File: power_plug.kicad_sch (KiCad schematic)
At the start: 21 parts, among them K13 Conn_02x03

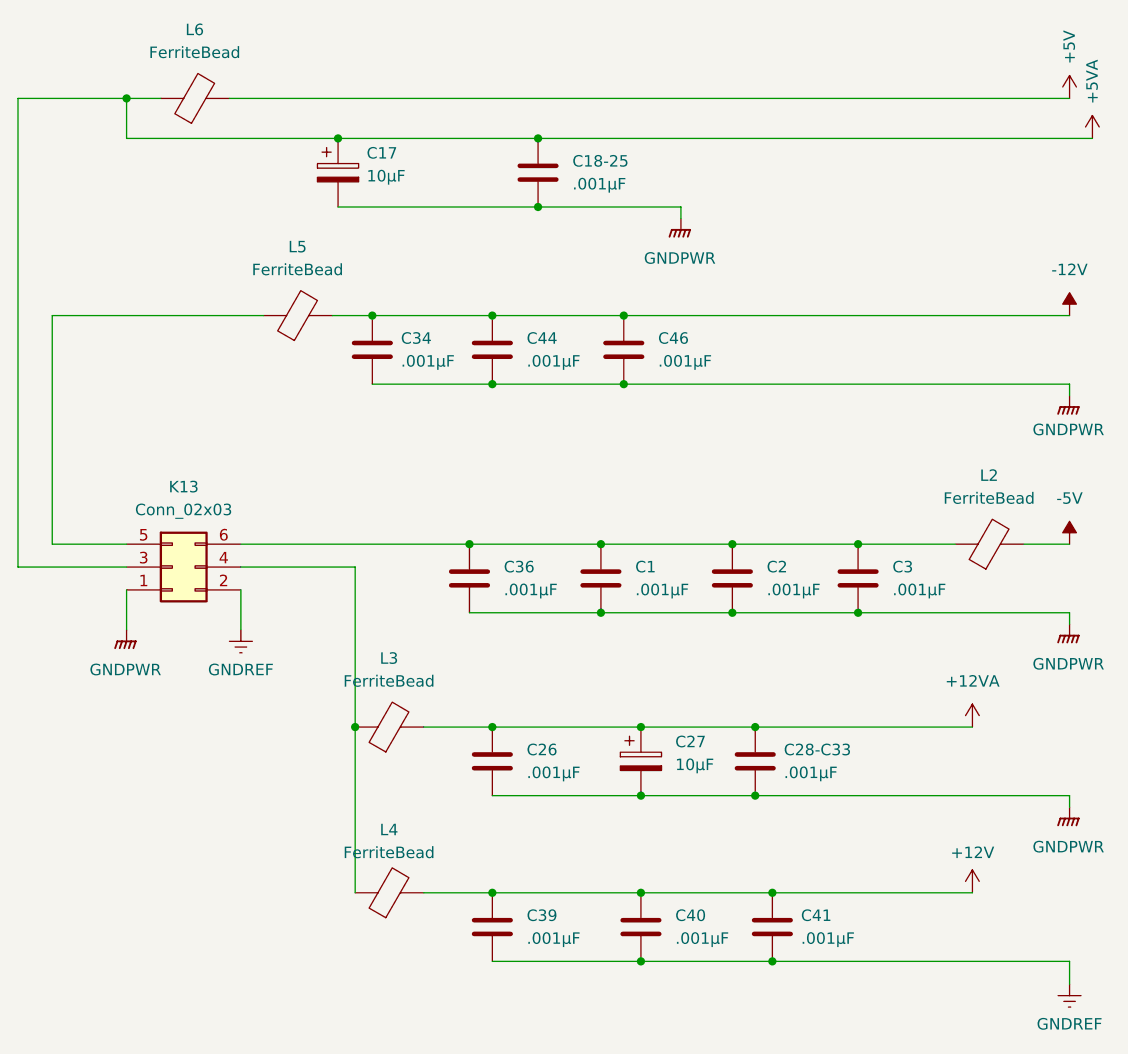
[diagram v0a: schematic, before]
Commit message: Use correct symbols
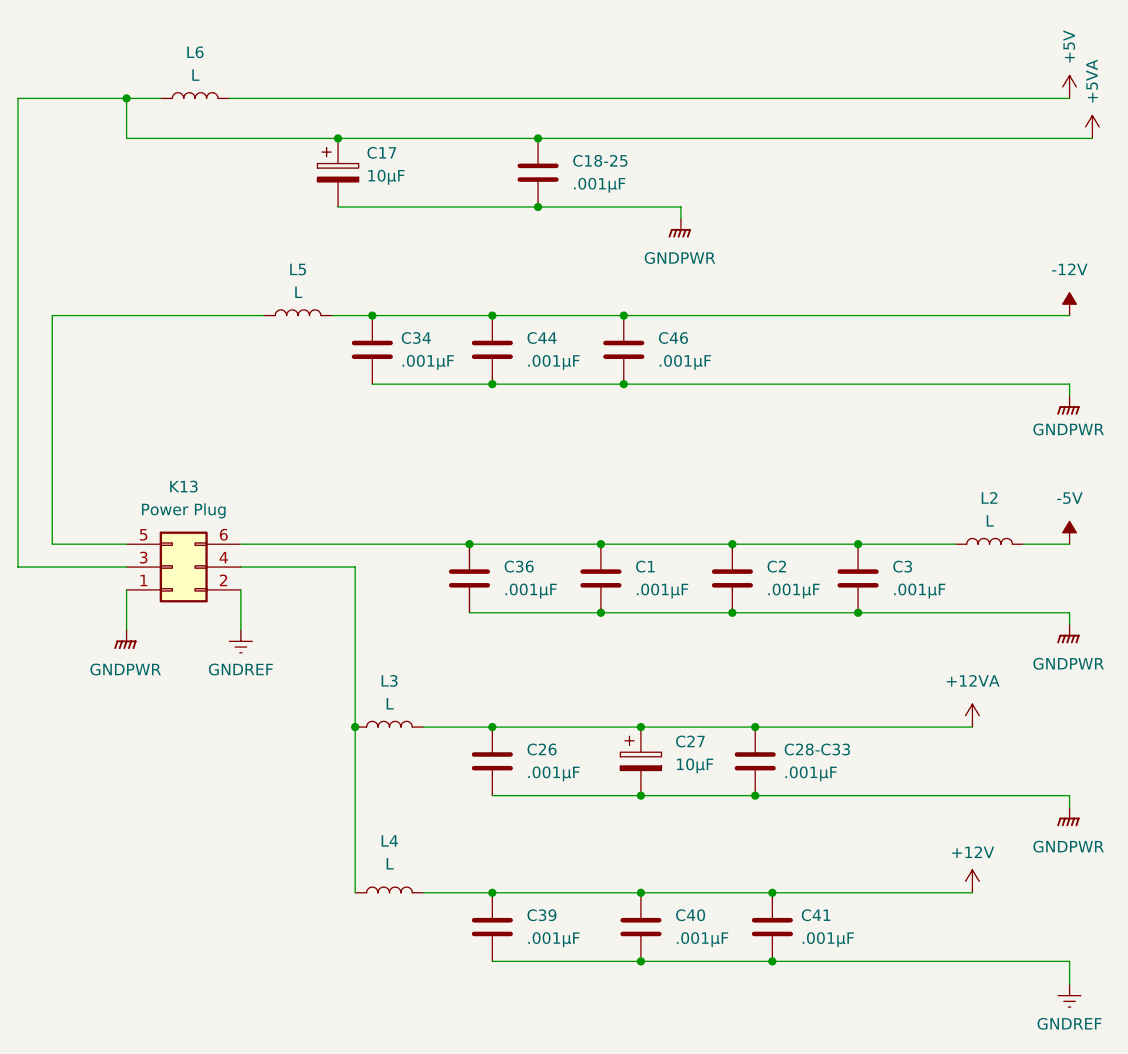
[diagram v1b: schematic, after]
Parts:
- removed L2, L3, L4, L5, L6: FerriteBead, symbol Device:FerriteBead
- added L2, L3, L4, L5, L6: L, symbol Device:L
- K13: value Conn_02x03 -> Power Plug
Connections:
- net +12V: now also L4.2
- net +12VA: now also L3.2
- net +5V: now also L6.2
- net +5VA: now also L6.1
- net -12V: now also L5.2
- net -5V: now also L2.2
- net at K13.4 (Pin_4): now also L3.1, L4.1
- net at K13.5 (Pin_5): now also L5.1
- net at C1.1, C2.1, C3.1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: now also L2.1
